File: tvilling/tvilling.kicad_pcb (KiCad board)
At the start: 2 copper layers, 78.7 x 73.7 mm, 10 parts, among them J1 Conn_01x05_Male, J2 Conn_01x05_Male, J3 Conn_01x05_Male, J4 Conn_01x05_Male, J5 Conn_01x02_Male, SW1 SW_SPST, U1 ESP32-devkit-v1, U2 TB6612_module, U3 TB6612_module

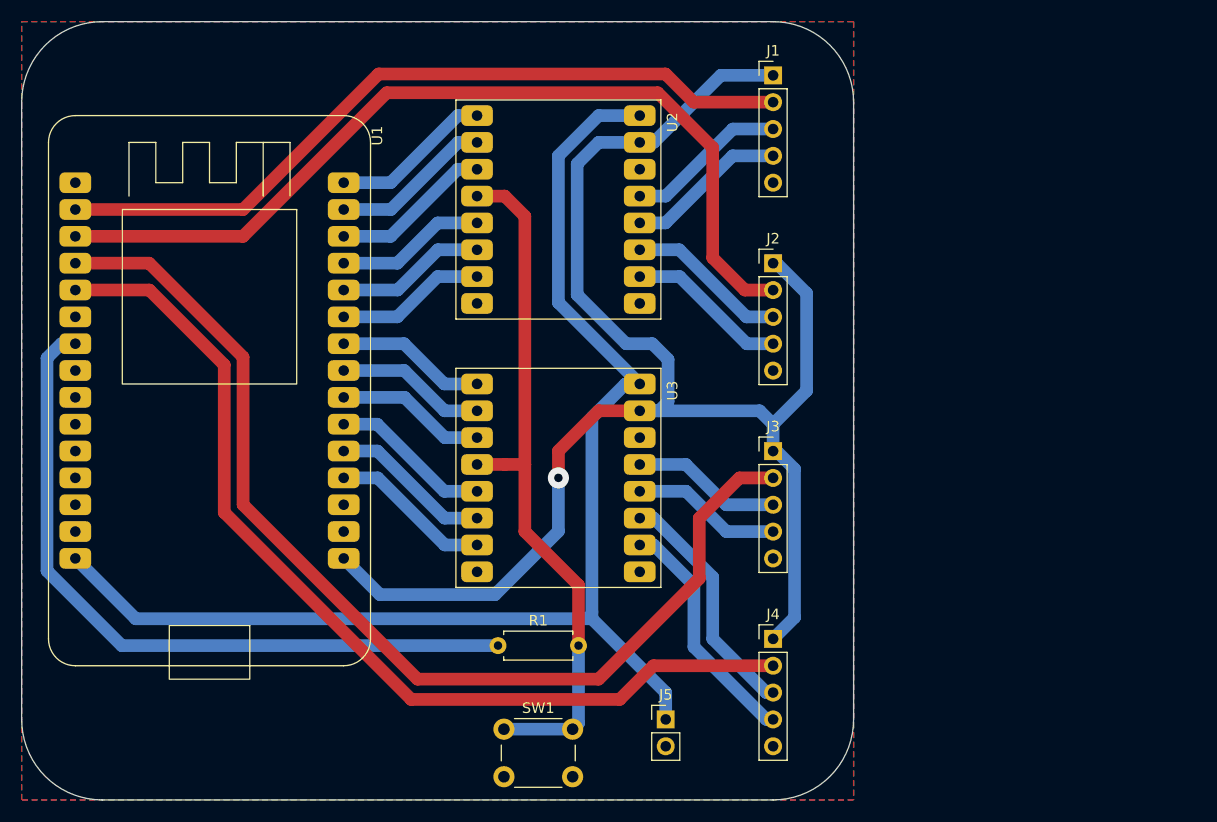
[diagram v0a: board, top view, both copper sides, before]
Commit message: Add button and leds for state indication
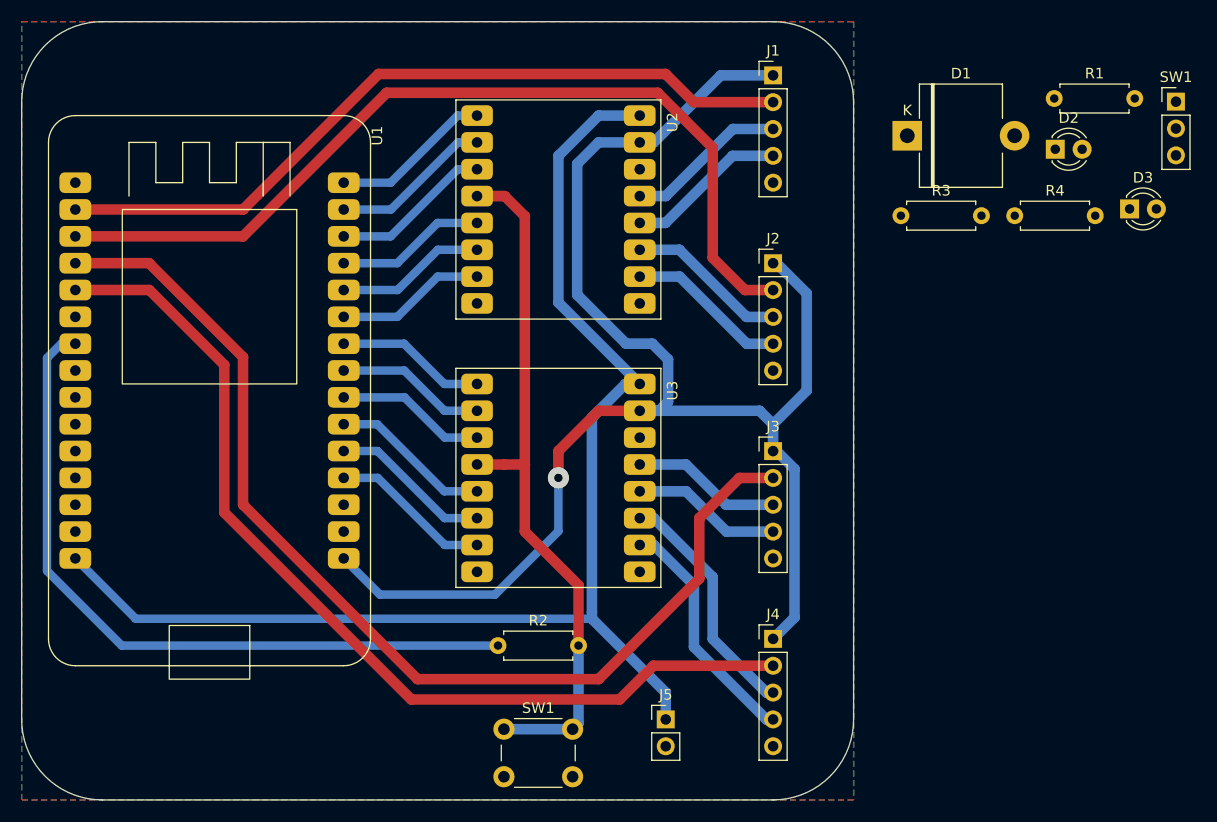
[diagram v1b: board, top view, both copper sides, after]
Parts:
- added D1: D_Zener, Diode_THT:D_5KP_P10.16mm_Horizontal, F.Cu at (165.1, 43.8)
- added D2: LED, LED_THT:LED_D3.0mm, F.Cu at (179.1, 45.1)
- added D3: LED, LED_THT:LED_D3.0mm, F.Cu at (186.1, 50.7)
- added R1: R, Resistor_THT:R_Axial_DIN0207_L6.3mm_D2.5mm_P7.62mm_Horizontal, F.Cu at (179.0, 40.3)
- added R3: R, Resistor_THT:R_Axial_DIN0207_L6.3mm_D2.5mm_P7.62mm_Horizontal, F.Cu at (164.5, 51.4)
- added R4: R, Resistor_THT:R_Axial_DIN0207_L6.3mm_D2.5mm_P7.62mm_Horizontal, F.Cu at (175.3, 51.4)
- added SW1: SW_SPDT, Connector_PinHeader_2.54mm:PinHeader_1x03_P2.54mm_Vertical, F.Cu at (190.5, 40.6)
- renumbered R1 to R2
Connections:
- J1 pad 1: +3.3V -> +1V1
- J2 pad 1: +3.3V -> +1V1
- J3 pad 1: +3.3V -> +1V1
- J4 pad 1: +3.3V -> +1V1
- R2 pad 1: /STBY -> VCC
- R2 pad 2: /STBY_D -> Net-(R2-Pad2)
- U2 pad 4: /STBY_D -> /STBY
- U3 pad 4: /STBY_D -> /STBY
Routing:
- net +3.3V: track 147.1 -> 0.00 mm, vias 1 -> 0
- net +1V1: track 0.00 -> 147.1 mm, vias 0 -> 1
- net VCC: track 122.6 -> 191.6 mm
- net /STBY_D: track 67.2 -> 0.00 mm
- net /STBY: track 69.0 -> 67.2 mm
